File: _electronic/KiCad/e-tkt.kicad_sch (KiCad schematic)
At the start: 1 part

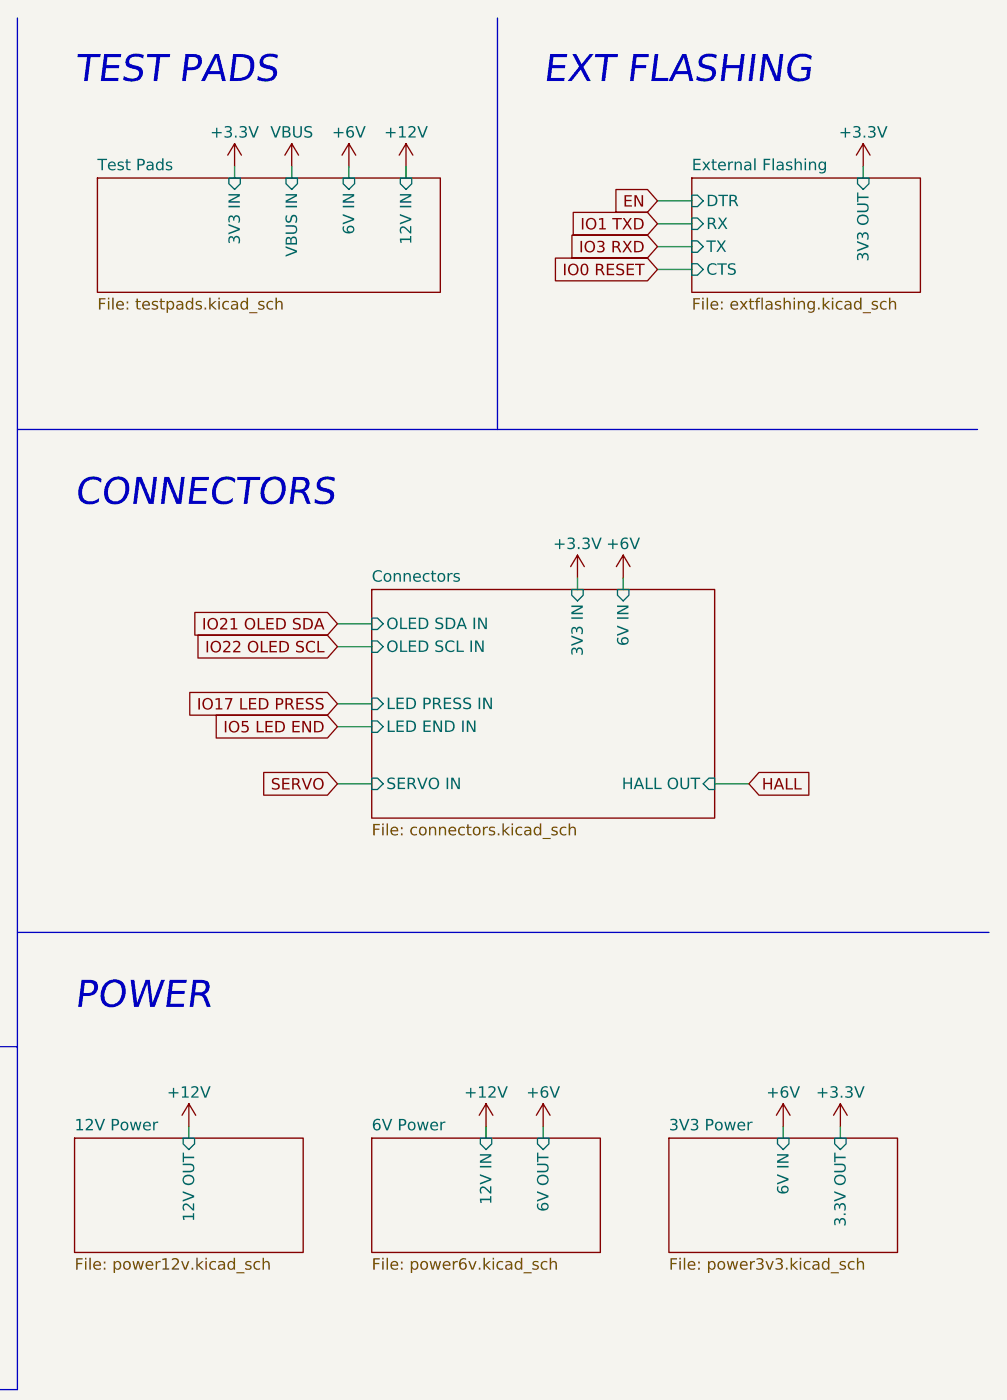
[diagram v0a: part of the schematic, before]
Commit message: external flashing header
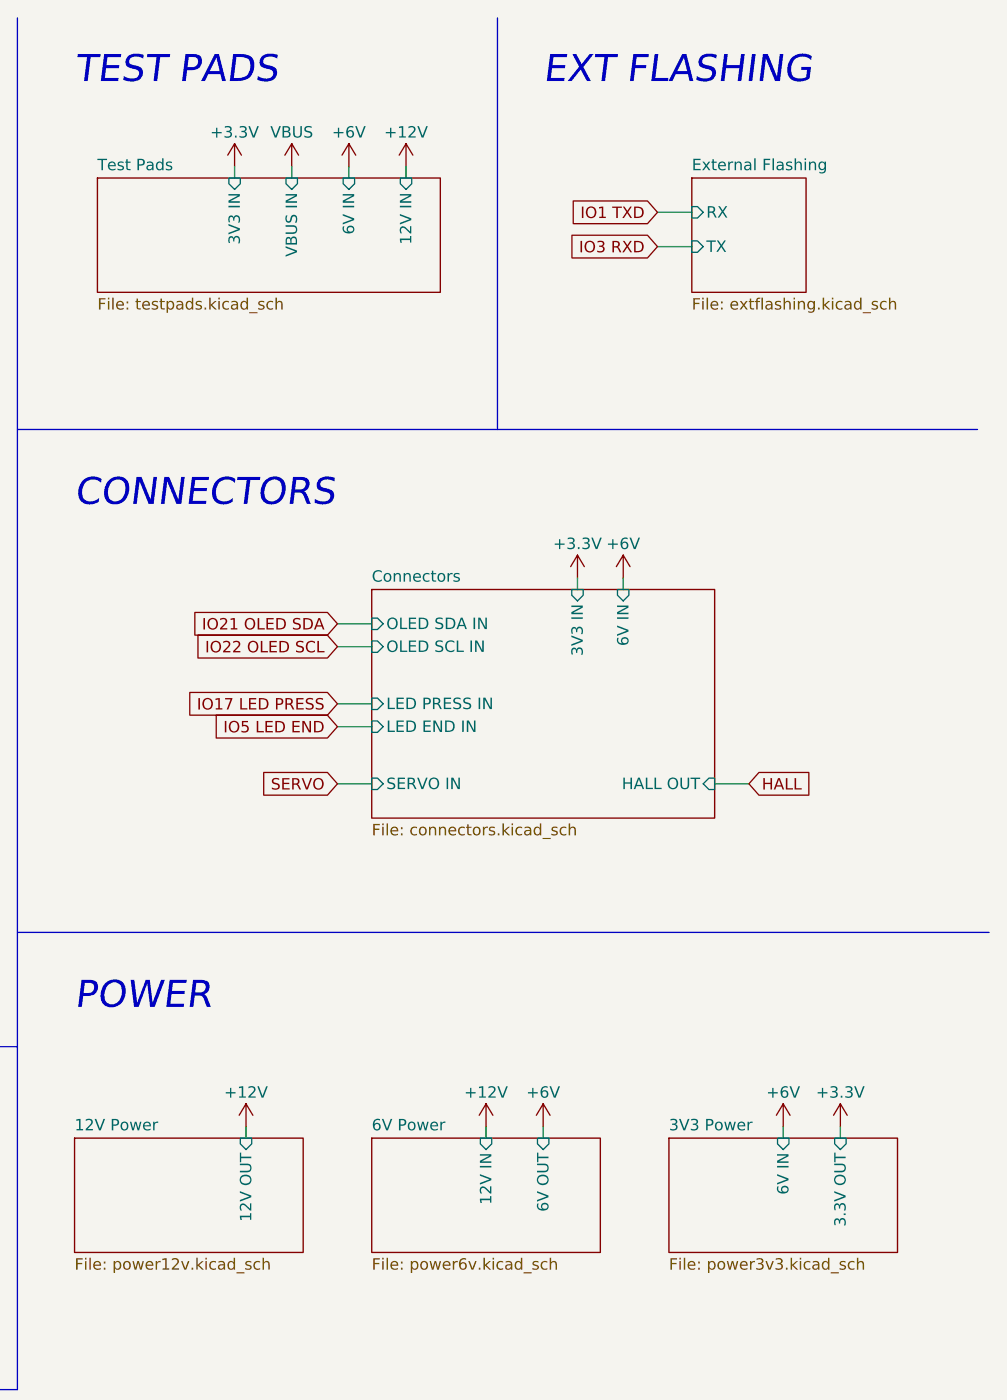
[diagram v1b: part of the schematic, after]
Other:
- sheet External Flashing ports: added none; removed 3V3 OUT, CTS, DTR
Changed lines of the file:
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@@
     (stroke (width 0) (type default) (color 0 0 0 0))
   )
-  (wire (pts (xy 196.85 135.89) (xy 196.85 137.16))
+  (wire (pts (xy 203.2 135.89) (xy 203.2 137.16))
     (stroke (width 0) (type default) (color 0 0 0 0))
   )
@@
     (stroke (width 0) (type default) (color 0 0 0 0))
   )
-  (wire (pts (xy 248.92 33.02) (xy 252.73 33.02))
-    (stroke (width 0) (type default) (color 0 0 0 0))
-  )
   (wire (pts (xy 245.11 74.93) (xy 245.11 76.2))
     (stroke (width 0) (type default) (color 0 0 0 0))
@@
     (stroke (width 0) (type default) (color 0 0 0 0))
   )
-  (wire (pts (xy 248.92 40.64) (xy 252.73 40.64))
-    (stroke (width 0) (type default) (color 0 0 0 0))
-  )
   (wire (pts (xy 149.86 80.01) (xy 153.67 80.01))
     (stroke (width 0) (type default) (color 0 0 0 0))
@@
     (stroke (width 0) (type default) (color 0 0 0 0))
   )
-  (wire (pts (xy 248.92 35.56) (xy 252.73 35.56))
+  (wire (pts (xy 248.92 34.29) (xy 252.73 34.29))
     (stroke (width 0) (type default) (color 0 0 0 0))
   )
@@
   )
   (wire (pts (xy 66.04 179.07) (xy 66.04 180.34))
-    (stroke (width 0) (type default) (color 0 0 0 0))
-  )
-  (wire (pts (xy 271.78 29.21) (xy 271.78 30.48))
     (stroke (width 0) (type default) (color 0 0 0 0))
   )
@@
     )
   )
-  (global_label "IO0 RESET" (shape input) (at 248.92 40.64 180) (fields_autoplaced)
-    (effects (font (size 1.27 1.27)) (justify right))
-    (property "Intersheet References" "${INTERSHEET_REFS}" (id 0) (at 236.6493 40.7194 0)
-      (effects (font (size 1.27 1.27)) (justify right) hide)
-    )
-  )
   (global_label "IO22 OLED SCL" (shape input) (at 213.36 82.55 180) (fields_autoplaced)
     (effects (font (size 1.27 1.27)) (justify right))
@@
     )
   )
-  (global_label "EN" (shape input) (at 248.92 33.02 180) (fields_autoplaced)
-    (effects (font (size 1.27 1.27)) (justify right))
-    (property "Intersheet References" "${INTERSHEET_REFS}" (id 0) (at 244.0274 33.0994 0)
-      (effects (font (size 1.27 1.27)) (justify right) hide)
-    )
-  )
   (global_label "IO4 ULN 2" (shape input) (at 111.76 185.42 180) (fields_autoplaced)
     (effects (font (size 1.27 1.27)) (justify right))
@@
     )
   )
-  (global_label "IO1 TXD" (shape input) (at 248.92 35.56 180) (fields_autoplaced)
-    (effects (font (size 1.27 1.27)) (justify right))
-    (property "Intersheet References" "${INTERSHEET_REFS}" (id 0) (at 238.9474 35.6394 0)
+  (global_label "IO1 TXD" (shape input) (at 248.92 34.29 180) (fields_autoplaced)
+    (effects (font (size 1.27 1.27)) (justify right))
+    (property "Intersheet References" "${INTERSHEET_REFS}" (id 0) (at 238.9474 34.3694 0)
       (effects (font (size 1.27 1.27)) (justify right) hide)
     )
@@
     (pin "1")
   )
-  (symbol (lib_id "power:+12V") (at 196.85 135.89 0) (unit 1)
-    (in_bom yes) (on_board yes)
-    (property "Reference" "#PWR0110" (id 0) (at 196.85 139.7 0)
-      (effects (font (size 1.27 1.27)) hide)
-    )
-    (property "Value" "+12V" (id 1) (at 196.85 132.08 0))
-    (property "Footprint" "" (id 2) (at 196.85 135.89 0)
-      (effects (font (size 1.27 1.27)) hide)
-    )
-    (property "Datasheet" "" (id 3) (at 196.85 135.89 0)
+  (symbol (lib_id "power:+12V") (at 203.2 135.89 0) (unit 1)
+    (in_bom yes) (on_board yes)
+    (property "Reference" "#PWR0110" (id 0) (at 203.2 139.7 0)
+      (effects (font (size 1.27 1.27)) hide)
+    )
+    (property "Value" "+12V" (id 1) (at 203.2 132.08 0))
+    (property "Footprint" "" (id 2) (at 203.2 135.89 0)
+      (effects (font (size 1.27 1.27)) hide)
+    )
+    (property "Datasheet" "" (id 3) (at 203.2 135.89 0)
       (effects (font (size 1.27 1.27)) hide)
     )
@@
     )
     (property "Datasheet" "" (id 3) (at 154.94 97.79 0)
-      (effects (font (size 1.27 1.27)) hide)
-    )
-    (pin "1")
-  )
-  (symbol (lib_id "power:+3.3V") (at 271.78 29.21 0) (unit 1)
-    (in_bom yes) (on_board yes)
-    (property "Reference" "#PWR0139" (id 0) (at 271.78 33.02 0)
-      (effects (font (size 1.27 1.27)) hide)
-    )
-    (property "Value" "+3.3V" (id 1) (at 271.78 25.4 0))
-    (property "Footprint" "" (id 2) (at 271.78 29.21 0)
-      (effects (font (size 1.27 1.27)) hide)
-    )
-    (property "Datasheet" "" (id 3) (at 271.78 29.21 0)
       (effects (font (size 1.27 1.27)) hide)
     )
@@
     )
   )
-  (sheet (at 252.73 30.48) (size 25.4 12.7) (fields_autoplaced)
+  (sheet (at 252.73 30.48) (size 12.7 12.7) (fields_autoplaced)
     (stroke (width 0.1524) (type solid) (color 0 0 0 0))
     (fill (color 0 0 0 0.0000))
@@
       (effects (font (size 1.27 1.27)) (justify left top))
     )
-    (pin "DTR" input (at 252.73 33.02 180)
-      (effects (font (size 1.27 1.27)) (justify left))
-    )
     (pin "TX" input (at 252.73 38.1 180)
       (effects (font (size 1.27 1.27)) (justify left))
     )
-    (pin "RX" input (at 252.73 35.56 180)
-      (effects (font (size 1.27 1.27)) (justify left))
-    )
-    (pin "CTS" input (at 252.73 40.64 180)
-      (effects (font (size 1.27 1.27)) (justify left))
-    )
-    (pin "3V3 OUT" input (at 271.78 30.48 90)
-      (effects (font (size 1.27 1.27)) (justify right))
+    (pin "RX" input (at 252.73 34.29 180)
+      (effects (font (size 1.27 1.27)) (justify left))
     )
   )
@@
       (effects (font (size 1.27 1.27)) (justify left top))
     )
-    (pin "12V OUT" input (at 196.85 137.16 90)
+    (pin "12V OUT" input (at 203.2 137.16 90)
       (effects (font (size 1.27 1.27)) (justify right))
     )
@@
       (reference "#PWR0138") (unit 1) (value "GNDREF") (footprint "")
     )
-    (path "/fb3de47a-ec92-4a82-8861-708420491674"
-      (reference "#PWR0139") (unit 1) (value "+3.3V") (footprint "")
-    )
     (path "/077b7f8a-3b82-46ad-b55a-a178b69955aa"
       (reference "#PWR0140") (unit 1) (value "+3.3V") (footprint "")
@@
       (reference "JP_SER1") (unit 1) (value "Bridged") (footprint "Jumper:SolderJumper-2_P1.3mm_Bridged2Bar_Pad1.0x1.5mm")
     )
-    (path "/500f785f-7d37-4530-93ef-964340f250e0/563cf8a3-be32-4f63-8e33-33d621fa1088"
-      (reference "JP_SER2") (unit 1) (value "Bridged") (footprint "Jumper:SolderJumper-2_P1.3mm_Bridged2Bar_Pad1.0x1.5mm")
-    )
     (path "/500f785f-7d37-4530-93ef-964340f250e0/1b89d775-bebb-467d-ab6a-2e6d4932732c"
       (reference "JP_SER3") (unit 1) (value "Bridged") (footprint "Jumper:SolderJumper-2_P1.3mm_Bridged2Bar_Pad1.0x1.5mm")
     )
-    (path "/500f785f-7d37-4530-93ef-964340f250e0/928eace1-ad42-4bba-a35b-7ecaeddfddfa"
-      (reference "JP_SER4") (unit 1) (value "Bridged") (footprint "Jumper:SolderJumper-2_P1.3mm_Bridged2Bar_Pad1.0x1.5mm")
-    )
     (path "/f455ead3-36df-4bbc-bff6-27228632d6c9/a802eff8-fd9f-41b4-924a-b1f72fec52a4"
       (reference "J_28byj-48-12v_1") (unit 1) (value "Conn_01x05_Male") (footprint "Connector_PinHeader_2.54mm:PinHeader_1x05_P2.54mm_Vertical")
     )
+    (path "/6b620b21-f9f4-45f9-ae29-09e80b0a55df/5fddb882-70ad-4f15-bda9-3a4789178dfd"
+      (reference "J_EXT1") (unit 1) (value "Conn_01x03_Male") (footprint "Connector_PinHeader_2.54mm:PinHeader_1x03_P2.54mm_Horizontal")
+    )
     (path "/7bf025fc-a57d-4f41-9c31-fcca97a0dd34/25fb1bc1-92f6-404a-b780-b416e13fa0fd"
       (reference "J_HALL1") (unit 1) (value "Conn_01x03_Female") (footprint "Connector_PinSocket_2.54mm:PinSocket_1x03_P2.54mm_Vertical")
@@
     )
     (path "/ab008ac4-72ad-4687-86ad-8fa342b57840/b8bcf044-d353-41cc-8e3f-28fe86d2ff58"
-      (reference "J_POW1") (unit 1) (value "Barrel_Jack_Switch") (footprint "Connector_BarrelJack:BarrelJack_GCT_DCJ200-10-A_Horizontal")
+      (reference "J_POW1") (unit 1) (value "Barrel_Jack_Switch") (footprint "SnapEDA Library:BarrelJack_GCT_DCJ200-10-A_Horizontal")
     )
     (path "/7bf025fc-a57d-4f41-9c31-fcca97a0dd34/755e457b-34fc-4fd1-b2c2-3fcae6bd5021"
@@
       (reference "TP_12v1") (unit 1) (value "TestPoint") (footprint "TestPoint:TestPoint_Pad_D1.0mm")
     )
-    (path "/6b620b21-f9f4-45f9-ae29-09e80b0a55df/f1f288ec-63ff-4c05-adee-5b9ae02c7c2e"
-      (reference "TP_CTS1") (unit 1) (value "TestPoint") (footprint "TestPoint:TestPoint_Pad_D1.0mm")
-    )
-    (path "/6b620b21-f9f4-45f9-ae29-09e80b0a55df/2aeee32a-07d6-405c-8f62-e86ea8d84299"
-      (reference "TP_DTR1") (unit 1) (value "TestPoint") (footprint "TestPoint:TestPoint_Pad_D1.0mm")
-    )
-    (path "/6b620b21-f9f4-45f9-ae29-09e80b0a55df/75047bec-8bc9-4bcc-b174-df5753f06a66"
-      (reference "TP_GND1") (unit 1) (value "TestPoint") (footprint "TestPoint:TestPoint_Pad_D1.0mm")
-    )
     (path "/80181399-56c9-4858-bcd2-be6de4dbffde/c13fc93a-0972-4a87-8f24-0804bf570334"
       (reference "TP_GND3") (unit 1) (value "TestPoint") (footprint "TestPoint:TestPoint_Pad_D1.0mm")
     )
-    (path "/6b620b21-f9f4-45f9-ae29-09e80b0a55df/a31ebef8-83bb-4a36-ab38-94620dfba0b1"
-      (reference "TP_RX1") (unit 1) (value "TestPoint") (footprint "TestPoint:TestPoint_Pad_D1.0mm")
-    )
-    (path "/6b620b21-f9f4-45f9-ae29-09e80b0a55df/56c9a772-893b-4dc5-8d85-a810fb42ab53"
-      (reference "TP_TX1") (unit 1) (value "TestPoint") (footprint "TestPoint:TestPoint_Pad_D1.0mm")
-    )
-    (path "/6b620b21-f9f4-45f9-ae29-09e80b0a55df/9f5139e1-ac28-4603-9466-743c97bd4904"
-      (reference "TP_VCC_3.3V1") (unit 1) (value "TestPoint") (footprint "TestPoint:TestPoint_Pad_D1.0mm")
-    )
     (path "/973f9b7f-d992-45f9-a125-51db85018136/fdecbef2-8cfc-4ede-8ea0-7a11182a7ade"
